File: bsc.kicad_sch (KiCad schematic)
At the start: 62 parts, among them J1 AVR-ISP-6, J11 Conn_02x05_Odd_Even, J2 Prog, J3 U0TXD silent, J4 Boot, K1 TIANBO-HJR-4102-L, Q1 BSS138, U1 LMO78_03-0.5, U2 ESP32WROOM32E16, U3 ATtiny24A-SS, U4 ADuM1201AR, U5 ADuM1201AR, U6 ADuM1201AR, U7 SN65HVD234, U8 SP3485EN, U9 SP3485EN, X1 Conn_S2, X2 Conn_S1, X4 Conn_SV

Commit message: Redesign PCB
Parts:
- removed C1: 10µ, Capacitor_SMD:CP_Elec_6.3x5.9, symbol Device:C_Small
- removed C12, C13, C14: 100n, Capacitor_SMD:C_0603_1608Metric, symbol Device:C_Small
- removed C6: 22µ, Capacitor_SMD:CP_Elec_6.3x5.9, symbol Device:C_Small
- removed D2: LED3, LED_SMD:LED_PLCC-2, symbol Device:LED_Small
- removed D3: LL4148, Diode_SMD:D_MiniMELF, symbol Diode:LL4148
- removed J1: AVR-ISP-6, Connector_PinHeader_2.54mm:PinHeader_2x03_P2.54mm_Vertical, symbol Connector:AVR-ISP-6
- removed J3: U0TXD silent, Connector_PinHeader_2.54mm:PinHeader_1x02_P2.54mm_Vertical, symbol Connector:Conn_01x02_Male
- removed JP5: O_SU2RXD, Jumper:SolderJumper-2_P1.3mm_Open_RoundedPad1.0x1.5mm, symbol Jumper:SolderJumper_2_Open
- removed JP6: O_SU2TXD, Jumper:SolderJumper-2_P1.3mm_Open_RoundedPad1.0x1.5mm, symbol Jumper:SolderJumper_2_Open
- removed K1: TIANBO-HJR-4102-L, Relay_THT:Relay_SPDT_HJR-4102, symbol Relay:TIANBO-HJR-4102-L
- removed Q1: BSS138, Package_TO_SOT_SMD:SOT-23, symbol Transistor_FET:BSS138
- removed R9: 180R, Resistor_SMD:R_0603_1608Metric, symbol Device:R_Small
- removed U3: ATtiny24A-SS, Package_SO:SOIC-14_3.9x8.7mm_P1.27mm, symbol MCU_Microchip_ATtiny:ATtiny24A-SS
- removed U4, U5, U6: ADuM1201AR, Package_SO:SOIC-8_3.9x4.9mm_P1.27mm, symbol Isolator:ADuM1201AR
- removed U8, U9: SP3485EN, Package_SO:SOIC-8_3.9x4.9mm_P1.27mm, symbol Interface_UART:SP3485EN
- removed X2: Conn_S1, Connector_Phoenix_MC:PhoenixContact_MCV_1,5_9-G-3.81_1x09_P3.81mm_Vertical, symbol Connector:Conn_01x09_Male
- added C1, C50, C52, C6: 100µ, Capacitor_SMD:CP_Elec_6.3x5.9, symbol Device:C_Polarized_Small
- added C12: 22µ, Capacitor_SMD:CP_Elec_4x5.8, symbol Device:C_Polarized_Small
- added C48, C51, C53, C54, C55: 100n, Capacitor_SMD:C_0603_1608Metric, symbol Device:C_Small
- added D11: LED1, LED_SMD:LED_PLCC-2, symbol Device:LED_Small
- added F1, F2: BELFUSE, Fuse:Fuse_0679H, symbol Device:Fuse_Small
- added H1, H2, H3, H4: MountingHole, MountingHole:MountingHole_3.2mm_M3, symbol Mechanical:MountingHole
- added J1: Conn_JTAG_ESP, Connector_PinHeader_1.27mm:PinHeader_2x10_P1.27mm_Vertical_SMD, symbol Connector_Generic:Conn_02x10_Odd_Even
- added JP28: 12V_5V, Jumper:SolderJumper-2_P1.3mm_Open_RoundedPad1.0x1.5mm, symbol Jumper:SolderJumper_2_Open
- added JP30: JP_EXT_5V, Jumper:SolderJumper-2_P1.3mm_Open_RoundedPad1.0x1.5mm, symbol Jumper:SolderJumper_2_Open
- added JP31: JP_EXT_3V3, Jumper:SolderJumper-2_P1.3mm_Open_RoundedPad1.0x1.5mm, symbol Jumper:SolderJumper_2_Open
- added PS1: 1S4E_0503S1U, custom_th:Converter_DCDC_GAPTEC_1S4E_S1U, symbol Converter_DCDC:MEE1S0303SC
- added Q1, Q13: BC857BS, Package_TO_SOT_SMD:SOT-363_SC-70-6, symbol Transistor_BJT:BC857BS
- added Q12, Q14: IRLML2244, Package_TO_SOT_SMD:SOT-23, symbol Transistor_FET:IRLML5203
- added R19: n.b., Resistor_SMD:R_0603_1608Metric, symbol Device:R_Small
- added R24: 180R, Resistor_SMD:R_0603_1608Metric, symbol Device:R_Small
- added U13: ADuM1201AR, Package_SO:SOIC-8_3.9x4.9mm_P1.27mm, symbol Isolator:ADuM1201AR
- added U19: LMO78_05-0.5, custom_th:Converter_DCDC_RECOM_R-78E-1.0, symbol Regulator_Switching:R-78E3.3-0.5
- C15, C16, C5, C8: value 100nF -> 100n
- C4: value 22µ -> 470µ/6,3V; footprint Capacitor_SMD:CP_Elec_6.3x5.9 -> Capacitor_SMD:CP_Elec_8x10; Reichelt (none) -> ECC MZL6R3ARA471
- J11: value Conn_02x05_Odd_Even -> Conn_Extension; footprint Connector_PinSocket_2.54mm:PinSocket_2x05_P2.54mm_Vertical -> Connector_PinHeader_2.54mm:PinHeader_2x05_P2.54mm_Vertical
- JP1: value O_U2RXD -> CAN_VCC
- JP2: value O_U2TXD -> CAN_GND
- JP3: value O_SU1RXD -> CAN_RC
- JP4: value O_SU1TXD -> CAN_TX
- R53, R54: value 10k -> n.b.
- R8: value 100k -> 10k
- U1: footprint Converter_DCDC:Converter_DCDC_RECOM_R-78E-0.5_THT -> custom_th:Converter_DCDC_RECOM_R-78E-1.0
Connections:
- net REL0_COM is gone; now on net +5V: X4.3 (Pin_3)
- net U1_VCC is gone; now on net GND: X1.1 (Pin_1)
- net +3V3: now also C8.1, C9.1, D1.2 (A), JP1.1 (A), R1.2, R2.2, X1.2 (Pin_2), C48.1, C54.1, C55.1, C6.1, JP31.1 (A), U13.1 (VDD1); no longer C10.1, C11.1, C16.1, C7.1, J11.8 (Pin_8), R1.1, R11.1, R2.1, R5.1, U7.3 (VCC)
- net +5V: now also C10.1, C7.1, C1.1, C52.1, C53.1, JP28.2 (B), JP30.1 (A), PS1.2 (+Vin), U19.3 (OUT); no longer J11.10 (Pin_10), X4.9 (Pin_9)
- net CAN_H: now also X1.4 (Pin_4); no longer X1.5 (Pin_5)
- net CAN_L: now also X1.5 (Pin_5); no longer X1.6 (Pin_6)
- net CAN_Rx: now also JP3.1 (A), U13.2 (VOA); no longer U7.4 (R)
- net CAN_Tx: now also JP4.1 (A), U13.3 (VIB); no longer U7.1 (D)
- net GND: now also C8.2, J11.1 (Pin_1), J11.3 (Pin_3), J11.5 (Pin_5), J11.7 (Pin_7), J11.9 (Pin_9), JP2.1 (A), R10.2, R5.2, R6.2, R7.2, C1.2, C48.2, C50.2, C51.2, C52.2, C53.2, C54.2, C55.2, C6.2, D11.1 (K), J1.10 (Pin_10), J1.12 (Pin_12), J1.14 (Pin_14), J1.16 (Pin_16), J1.18 (Pin_18), J1.20 (Pin_20), J1.4 (Pin_4), J1.6 (Pin_6), J1.8 (Pin_8), PS1.1 (-Vin), U13.4 (GND1), U19.2 (GND); no longer C11.2, C15.2, C16.2, C8.1, D1.1 (K), D4.3 (A), R12.1, R6.1, U7.2 (GND), X4.8 (Pin_8)
- net H_CLK: now also J1.7 (Pin_7); no longer J11.1 (Pin_1)
- net H_MISO: now also J1.5 (Pin_5)
- net H_MOSI: now also J1.9 (Pin_9)
- net INPUT/IO_DATA_OUT: no longer J11.5 (Pin_5)
- net INPUT/IO_DI_PL: no longer J11.7 (Pin_7)
- net OUTPUT/IO_DATA_IN: no longer J11.3 (Pin_3)
- net RST_ESP: now also R1.1, J1.3 (Pin_3); no longer R1.2
- net SCL: no longer X1.8 (Pin_8)
- net SDA: no longer X1.9 (Pin_9)
- net U1RX: no longer JP1.1 (A)
- net U1RX_O: now also X1.9 (Pin_9); no longer JP1.2 (B), X1.4 (Pin_4)
- net U1TX: no longer JP2.1 (A)
- net U1TX_O: now also X1.8 (Pin_8); no longer JP2.2 (B), X1.3 (Pin_3)
- net U1_GND: now also X1.7 (Pin_7); no longer X1.2 (Pin_2)
- net U3RX: no longer JP3.1 (A)
- net U3TX: no longer JP4.1 (A)
- net onewire: now also R2.1, X1.3 (Pin_3); no longer R2.2, X1.7 (Pin_7)
- net at R8.1: now also Q13.3 (C2), Q14.1 (G)
- net at R7.1: now also Q13.2 (B1), Q13.5 (B2), Q13.6 (C1); no longer R6.2
- net at R10.1: now also D1.1 (K); no longer D1.2 (A)
- net TACHO: now reaches U2.12 (IO27)
- net TACHO: no longer J11.9 (Pin_9)
- net T_ADDR2: now reaches U2.23 (IO15)
- net T_ADDR2: now also J1.13 (Pin_13)
- net LED1: now reaches J4.1 (Pin_1), U2.25 (IO0)
- net LED1: now also R24.2
- removed net AVR_RST: C9.1, R5.2
- net REL0_NC renamed V_IN
- net V_IN: now also C50.1, C51.1, JP28.1 (A), Q1.4 (E2), Q12.2 (S), Q13.4 (E2), Q14.2 (S), U19.1 (IN)
- net REL0_NO renamed AI1
- net U3RX_O renamed CAN_Rx_s
- net CAN_Rx_s: now also U7.4 (R), U13.7 (VIA)
- net U3TX_O renamed CAN_Tx_s
- net CAN_Tx_s: now also U7.1 (D), U13.6 (VOB)
- net WDT_TRIG_ESP_OUT renamed U2RXTX_EN
- net WDT_TRIG__ESP_IN renamed AI1d
- new net: J11.10 (Pin_10), JP30.2 (B)
- new net: F2.2, Q13.1 (E1), Q14.3 (D)
- new net: Q1.3 (C2), Q12.1 (G), R6.1
- new net: Q1.2 (B1), Q1.5 (B2), Q1.6 (C1), R5.1
- new net: F1.2, Q1.1 (E1), Q12.3 (D)
- new net: D11.2 (A), R24.1
- new net: J11.8 (Pin_8), JP31.2 (B)
- new net CAN_GND: C11.2, C12.2, C15.2, C16.2, D4.3 (A), JP2.2 (B), PS1.3 (-Vout), R12.1, R19.1, U13.5 (GND2), U7.2 (GND)
- new net CAN_VCC: C11.1, C12.1, C16.1, JP1.2 (B), PS1.4 (+Vout), R11.1, R19.2, U13.8 (VDD2), U7.3 (VCC)
- new net U1_VCC_e: X1.6 (Pin_6)
- new net V_IN1: F1.1, X4.9 (Pin_9)
- new net V_IN2: F2.1, X4.8 (Pin_8)
- no-connect marks 8 -> 16
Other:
- added sheet Analogeingänge (ai.kicad_sch)
- added sheet serial (serial.kicad_sch)
- sheet OUTPUT ports: added TACHO, T_ADDR2; removed none
- note added: "Alternativbestückung 5V/12V - Wenn 12V intern benötigt werden U19 bestücken. - Werden keine 12V benötigt U19 NICHT bestücken und mit JP28 überbrücken."
- note added: "Alternativtypen U7: SN65HVD230 (R11 darf nicht bestückt werden!) SN65HVD231 (R11 darf nicht bestückt werden!)"
- note added: "CAN"
- note added: "CAN_VCC = 3V3"
- note added: "JTAG: TDI=H_MISO TMS=H_CLK TCK=H_MOSI TDO=T_ADDR2"
- note removed: "Jumper zum direkt herausführen der Seriellen-SS"
- note removed: "Pins HIGH bei Boot Einige GPIOs wechseln beim Booten oder beim Reset ihren Status zu HIGH oder geben PWM-Signale aus. Für möglicherweise angeschlossene Peripherie bedeutet dies, dass es bei ihnen dann zu unerwartetem Verhalten kommen kann. - GPIO1 - GPIO3 - GPIO5 GPIO6 bis GPIO11 Diese sind mit dem ESP32-integrierten SPI Flash Memory verbunden und sollten deshalb nicht benutzt werden."
- moved on the sheet: C16, C2, C3, C4, C5, D1, D4, J11, J2, J4, R1, R10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

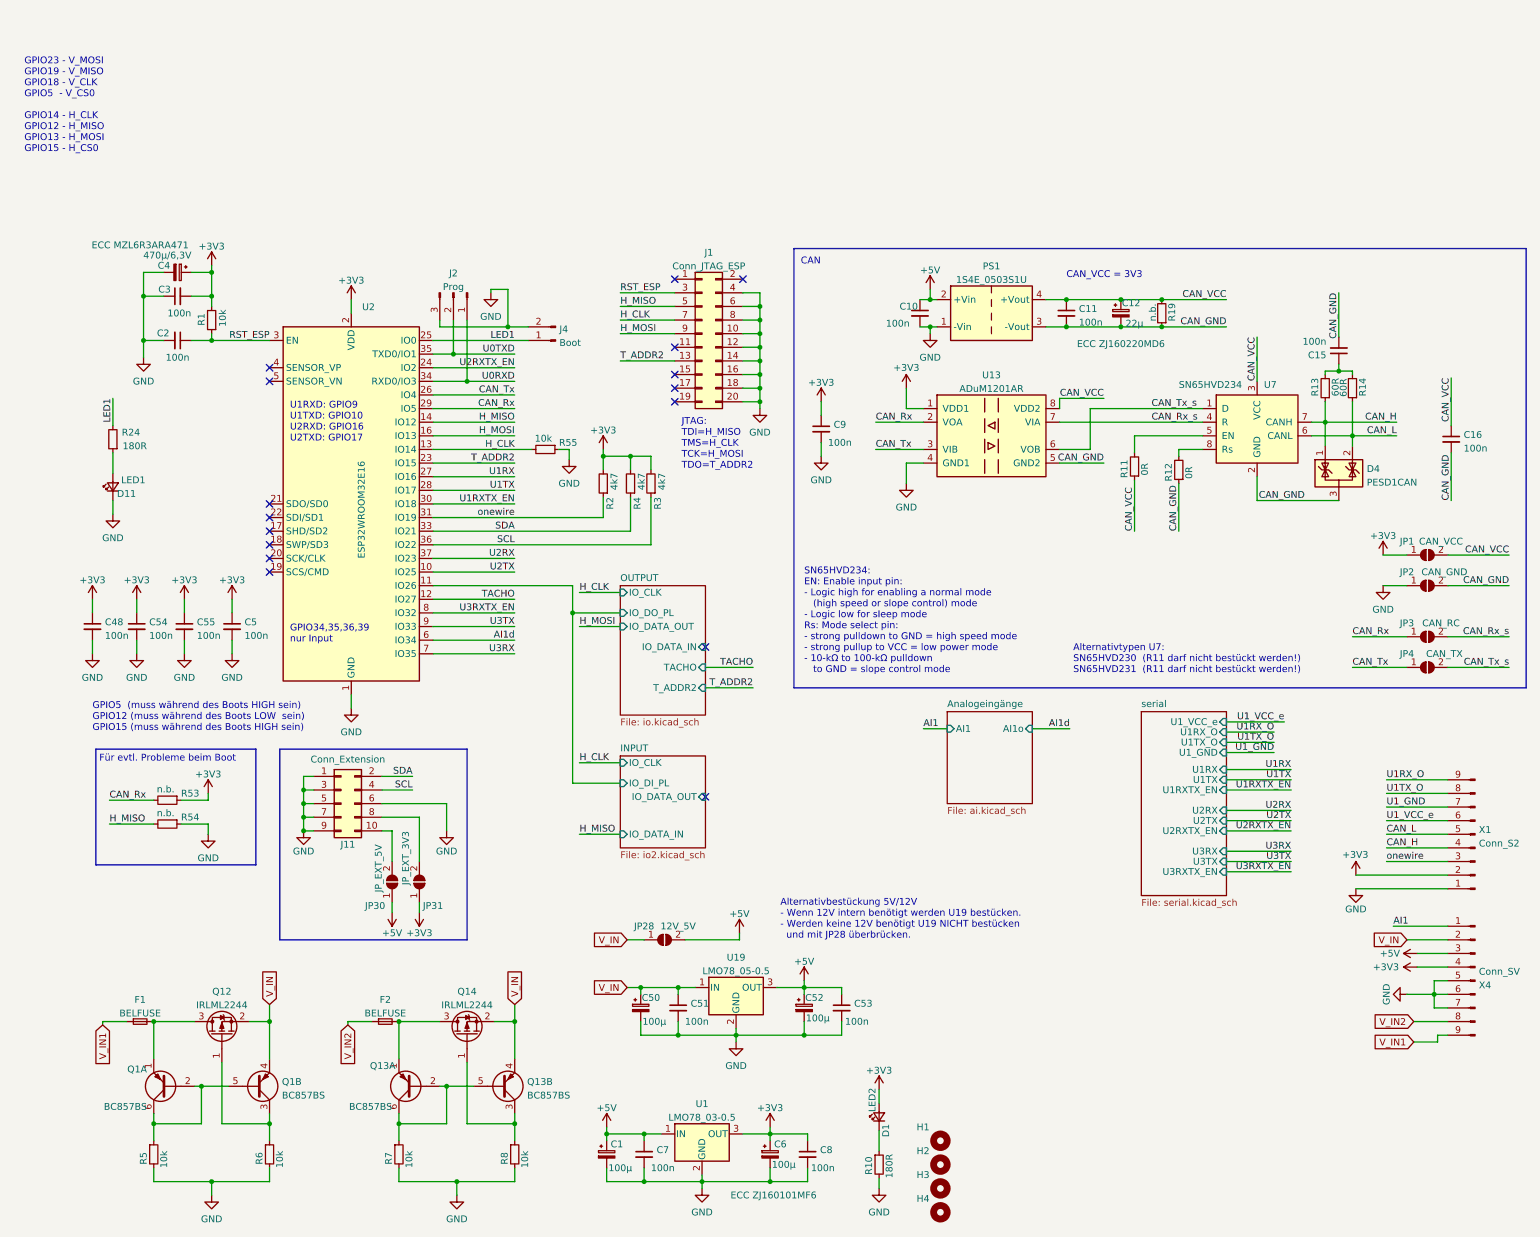
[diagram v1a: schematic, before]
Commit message: Layout optimized
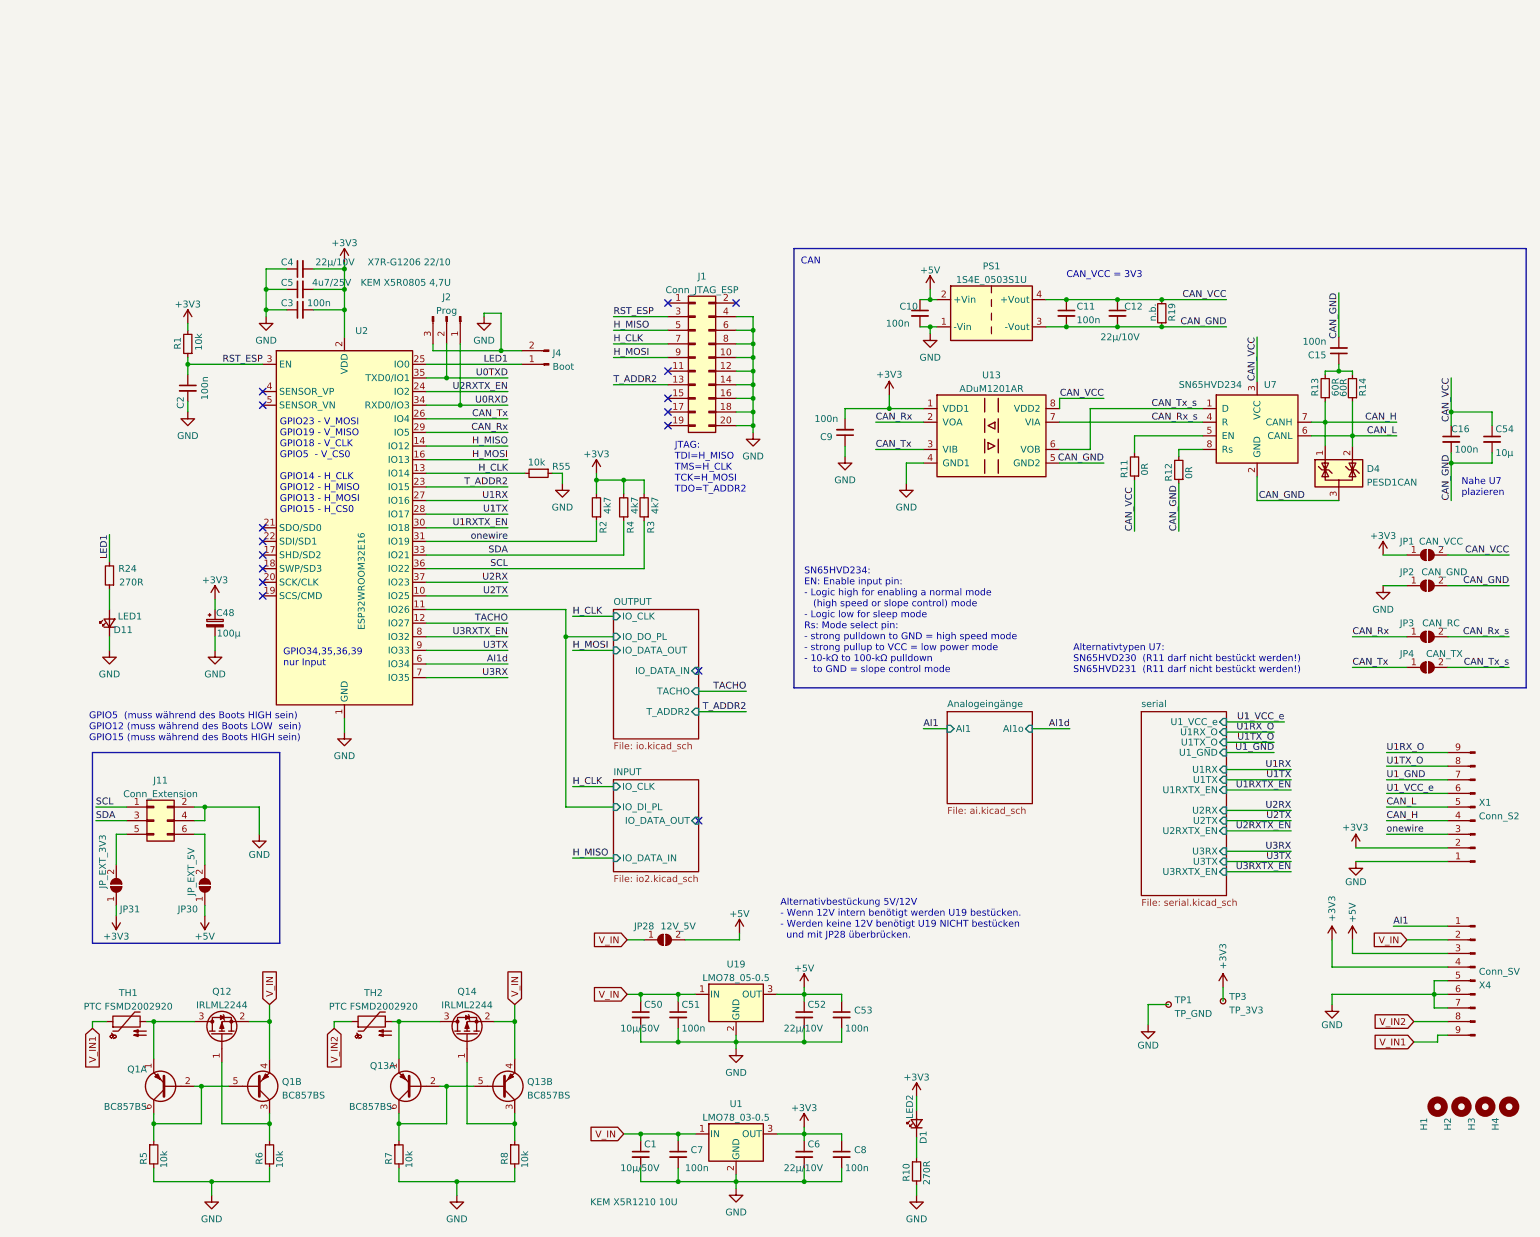
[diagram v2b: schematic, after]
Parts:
- removed C1, C50, C52, C6: 100µ, Capacitor_SMD:CP_Elec_6.3x5.9, symbol Device:C_Polarized_Small
- removed C12: 22µ, Capacitor_SMD:CP_Elec_4x5.8, symbol Device:C_Polarized_Small
- removed C4: 470µ/6,3V, Capacitor_SMD:CP_Elec_8x10, symbol Device:C_Polarized_Small
- removed C48, C55: 100n, Capacitor_SMD:C_0603_1608Metric, symbol Device:C_Small
- removed F1, F2: BELFUSE, Fuse:Fuse_0679H, symbol Device:Fuse_Small
- removed J11: Conn_Extension, Connector_PinHeader_2.54mm:PinHeader_2x05_P2.54mm_Vertical, symbol Connector_Generic:Conn_02x05_Odd_Even
- removed R53, R54: n.b., Resistor_SMD:R_0603_1608Metric, symbol Device:R_Small
- added C1, C50: 10µ/50V, Capacitor_SMD:C_1206_3216Metric, symbol Device:C_Small
- added C12, C52, C6: 22µ/10V, Capacitor_SMD:C_1206_3216Metric, symbol Device:C_Small
- added C4: 22µ/10V, Capacitor_SMD:C_0805_2012Metric, symbol Device:C_Small
- added C48: 100µ, Capacitor_SMD:CP_Elec_6.3x5.9, symbol Device:C_Polarized_Small
- added J11: Conn_Extension, Connector_PinHeader_2.54mm:PinHeader_2x03_P2.54mm_Vertical, symbol Connector_Generic:Conn_02x03_Odd_Even
- added TH1, TH2: PTC FSMD2002920, Fuse:Fuse_2920_7451Metric, symbol Device:Thermistor_PTC
- added TP1: TP_GND, TestPoint:TestPoint_Pad_1.0x1.0mm, symbol Connector:TestPoint_Small
- added TP3: TP_3V3, TestPoint:TestPoint_Pad_1.0x1.0mm, symbol Connector:TestPoint_Small
- C5: value 100n -> 4u7/25V; footprint Capacitor_SMD:C_0603_1608Metric -> Capacitor_SMD:C_0805_2012Metric; Reichelt (none) -> KEM X5R0805 4,7U
- C54: value 100n -> 10µ; footprint Capacitor_SMD:C_0603_1608Metric -> Capacitor_SMD:C_0805_2012Metric
- D1, D11: footprint LED_SMD:LED_PLCC-2 -> LED_SMD:LED_0603_1608Metric
- R10, R24: value 180R -> 270R
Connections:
- net +3V3: now also C5.2, C9.2, C4.2, C48.1, C6.1, TP3.1; no longer C5.1, C54.1, C9.1
- net +5V: now also C52.1; no longer C7.1, U1.1 (IN)
- net CAN_GND: now also C54.2, C12.2
- net CAN_VCC: now also C54.1, C12.1
- net GND: now also C5.1, C9.1, C1.2, C4.1, C48.2, C50.2, C52.2, C6.2, J11.2 (Pin_2), J11.4 (Pin_4), TP1.1; no longer C5.2, C54.2, C9.2
- net SCL: now also J11.1 (Pin_1)
- net SDA: now also J11.3 (Pin_3)
- net V_IN: now also C7.1, U1.1 (IN), C1.1, C50.1
- net V_IN1: now also TH1.1
- net V_IN2: now also TH2.1
- net at JP30.2 (B): now also J11.6 (Pin_6)
- net at Q13.1 (E1), Q14.3 (D): now also TH2.2
- net at Q1.1 (E1), Q12.3 (D): now also TH1.2
- net at JP31.2 (B): now also J11.5 (Pin_5)
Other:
- note added: "Nahe U7 plazieren"
- note removed: "Für evtl. Probleme beim Boot"
- note removed: "U1RXD: GPIO9 U1TXD: GPIO10 U2RXD: GPIO16 U2TXD: GPIO17"
- moved on the sheet: C2, C3, C51, C53, C7, C8, C9, D1, D11, H1, H2, H3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

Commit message: Change extension bus
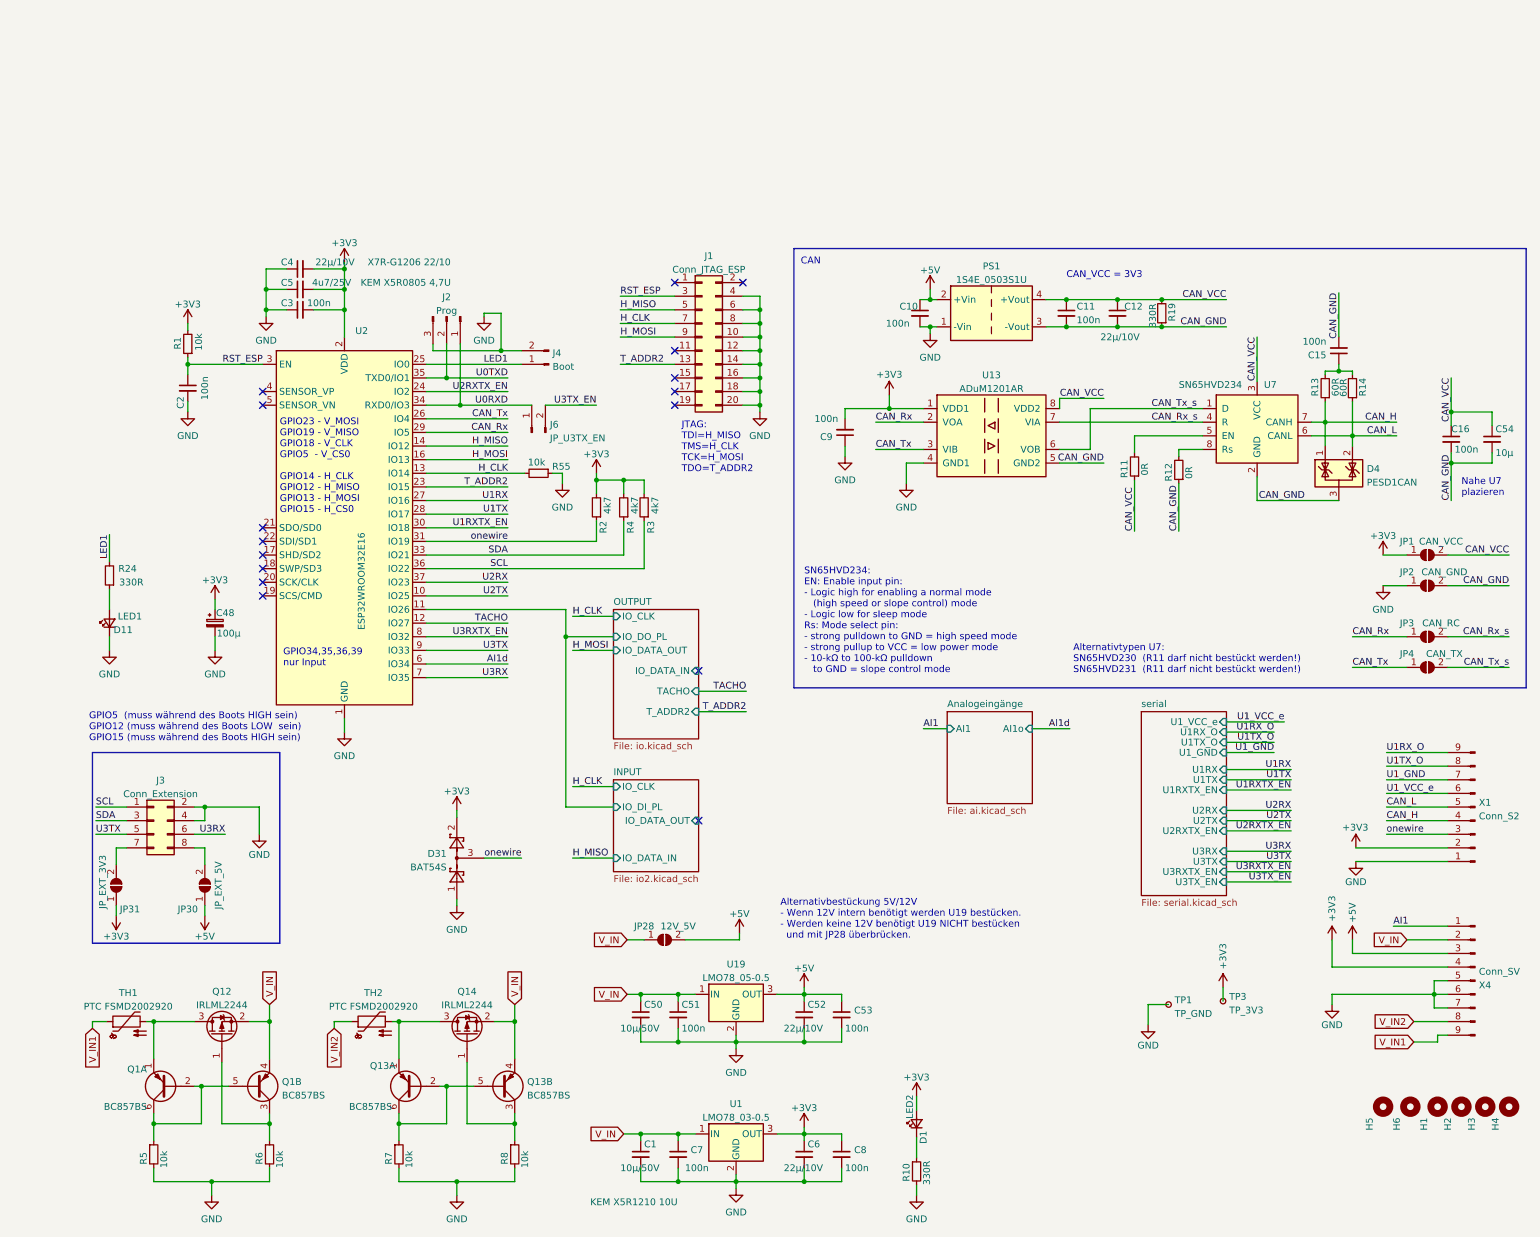
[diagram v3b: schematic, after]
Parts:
- removed J11: Conn_Extension, Connector_PinHeader_2.54mm:PinHeader_2x03_P2.54mm_Vertical, symbol Connector_Generic:Conn_02x03_Odd_Even
- added D31: BAT54S, Package_TO_SOT_SMD:SOT-23, symbol Diode:BAT54S
- added H5, H6: MountingHole, MountingHole:MountingHole_3.2mm_M3, symbol Mechanical:MountingHole
- added J3: Conn_Extension, bsc_custom:PinHeader_2x04_P2.54mm_Vertical_jlc, symbol Connector_Generic:Conn_02x04_Odd_Even
- added J6: JP_U3TX_EN, bsc_custom:PinHeader_1x02_P2.54mm_Vertical_jlc, symbol Connector:Conn_01x02_Male
- C4: footprint Capacitor_SMD:C_0805_2012Metric -> Capacitor_SMD:C_1206_3216Metric
- J2: footprint Connector_PinHeader_2.54mm:PinHeader_1x03_P2.54mm_Vertical -> custom_th:PinHeader_1x03_P2.54mm_Vertical_jlc
- J4: footprint Connector_PinHeader_2.54mm:PinHeader_1x02_P2.54mm_Vertical -> bsc_custom:PinHeader_1x02_P2.54mm_Vertical_jlc
- R10, R24: value 270R -> 330R
- R19: value n.b. -> 330R
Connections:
- net +3V3: now also D31.2
- net GND: now also D31.1, J3.2 (Pin_2), J3.4 (Pin_4)
- net SCL: now also J3.1 (Pin_1)
- net SDA: now also J3.3 (Pin_3)
- net U0RXD: now also J6.1 (Pin_1)
- net U3RX: now also J3.6 (Pin_6)
- net U3TX: now also J3.5 (Pin_5)
- net onewire: now also D31.3
- net at JP30.2 (B): now also J3.8 (Pin_8)
- net at JP31.2 (B): now also J3.7 (Pin_7)
- new net U3TX_EN: J6.2 (Pin_2)
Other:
- sheet serial ports: added U3TX_EN; removed none
- moved on the sheet: J1
